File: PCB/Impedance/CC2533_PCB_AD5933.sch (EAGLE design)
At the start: 34 parts

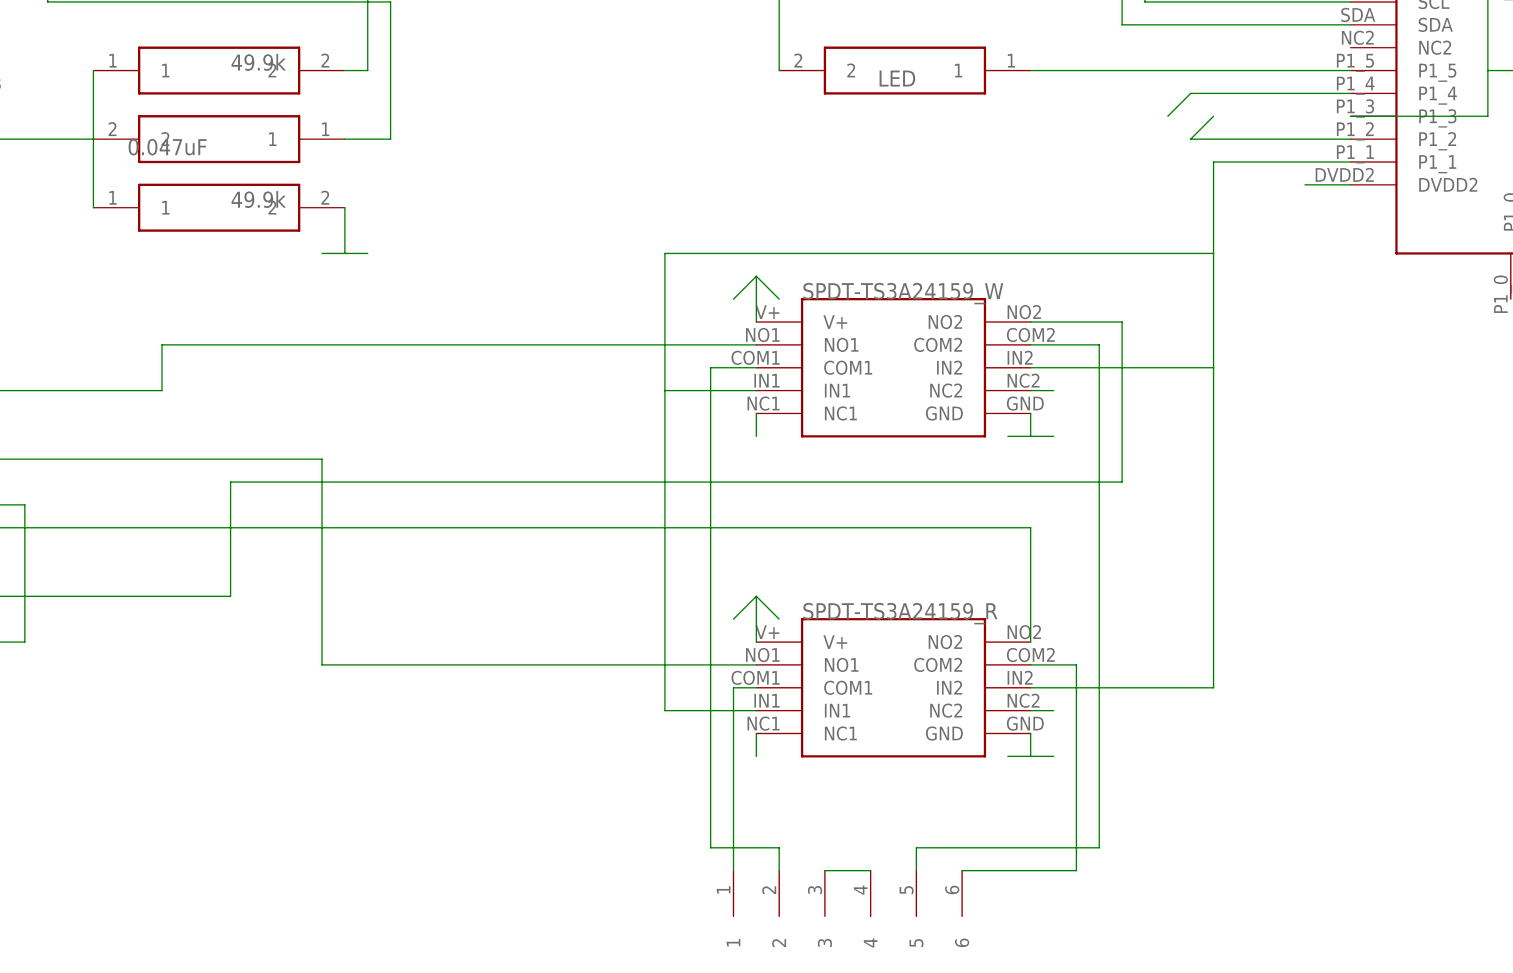
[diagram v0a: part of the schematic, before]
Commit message: New updates
Added new layout of CC2533 voltage stim and AD5933 impeance analysis
with ground planes (completed), and that of AD5933 impedance analysis
only.
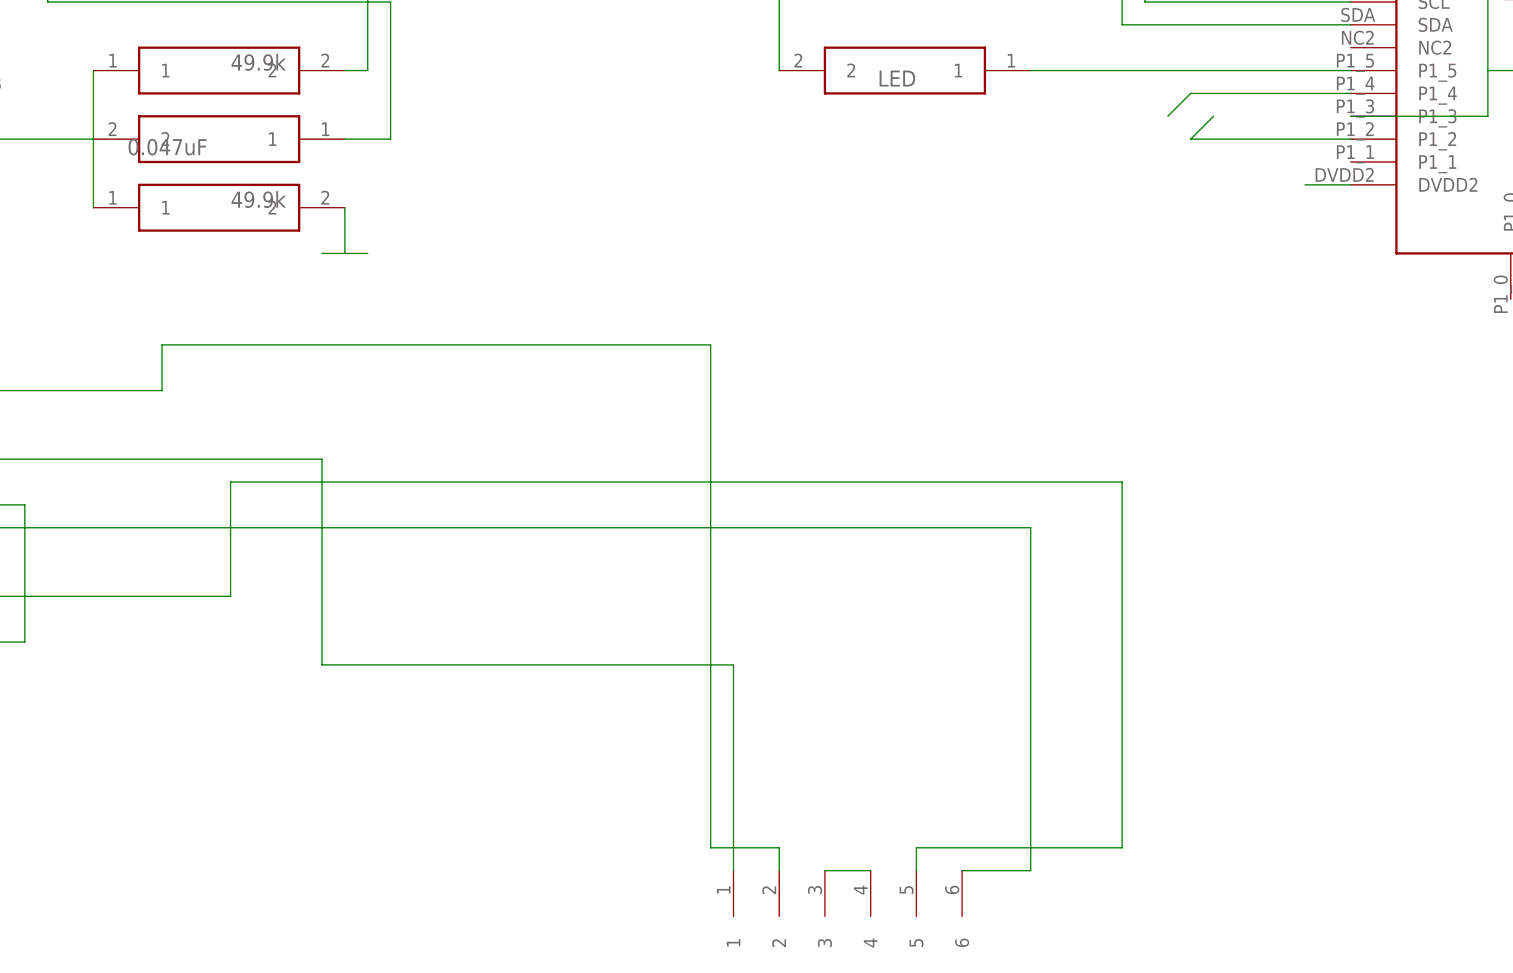
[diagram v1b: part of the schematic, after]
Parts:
- removed U$13, U$15: SPDT_DUAL, CC2530_PCB_TL:SPDT_DUAL
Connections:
- removed net IN1: U$1.P1_1, U$13.IN1, U$13.IN2, U$15.IN1, U$15.IN2
- removed net N$15: U$15.COM1, U$30.2
- removed net N$30: U$15.COM2, U$30.5
- removed net N$31: U$13.NO1, U$19.NO2
- removed net N$32: U$13.NO2, U$19.NC2
- net GND: no longer U$13.GND, U$15.GND
- net LEFT: no longer U$15.NC1
- net N$10: now also U$19.NC2; no longer U$13.COM2
- net N$7: now also U$30.2; no longer U$15.NO1
- net N$8: now also U$30.5; no longer U$15.NO2
- net N$9: now also U$19.NO2; no longer U$13.COM1
- net P0_1: no longer U$13.NC1
- net P0_3: no longer U$13.NC2
- net RIGHT: no longer U$15.NC2
- net VDD: no longer U$13.V+, U$15.V+

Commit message: Complete layouts for CC2533 circuits with AD5933
CC2533_PCB_Main_Plane - Voltage stim + Impedance Analysis.
CC2533_PCB_Biphasic - Current stim + Impedance Analysis.
CC2533_PCB_AD5933 - Impedance Analysis only.
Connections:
- net IN2: now also U$1.P2_0; no longer U$1.P1_6
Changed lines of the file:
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@@
 <net name="IN2" class="0">
 <segment>
-<pinref part="U$1" gate="G$1" pin="P1_6"/>
-<wire x1="68.58" y1="81.28" x2="68.58" y2="96.52" width="0.1524" layer="91"/>
-<wire x1="68.58" y1="96.52" x2="55.88" y2="96.52" width="0.1524" layer="91"/>
-<wire x1="55.88" y1="96.52" x2="55.88" y2="99.06" width="0.1524" layer="91"/>
-<wire x1="55.88" y1="99.06" x2="50.8" y2="99.06" width="0.1524" layer="91"/>
-<wire x1="50.8" y1="99.06" x2="50.8" y2="93.98" width="0.1524" layer="91"/>
-<wire x1="50.8" y1="93.98" x2="55.88" y2="93.98" width="0.1524" layer="91"/>
-<wire x1="55.88" y1="93.98" x2="55.88" y2="96.52" width="0.1524" layer="91"/>
+<wire x1="63.5" y1="99.06" x2="58.42" y2="99.06" width="0.1524" layer="91"/>
+<wire x1="58.42" y1="99.06" x2="58.42" y2="93.98" width="0.1524" layer="91"/>
+<wire x1="58.42" y1="93.98" x2="63.5" y2="93.98" width="0.1524" layer="91"/>
+<wire x1="63.5" y1="93.98" x2="63.5" y2="96.52" width="0.1524" layer="91"/>
+<pinref part="U$1" gate="G$1" pin="P2_0"/>
+<wire x1="63.5" y1="96.52" x2="63.5" y2="99.06" width="0.1524" layer="91"/>
+<wire x1="63.5" y1="96.52" x2="73.66" y2="96.52" width="0.1524" layer="91"/>
+<wire x1="73.66" y1="96.52" x2="73.66" y2="81.28" width="0.1524" layer="91"/>
 </segment>
 <segment>
